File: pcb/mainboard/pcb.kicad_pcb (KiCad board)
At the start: 4 copper layers, 67 x 58 mm, 146 parts, among them J101 Conn_01x04, J400 AudioJack3_SwitchT, J801 USB_B_Mini, U1 AXP209, U201 MIMXRT1176DVMAA, U400 CS43130, U401 ADP150-1.8, U402 ADP150-1.8, U404 MT48H16M32LFB5-6 or IS42VM321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, U700 W25Q128JVP, U800 USBLC6-2P6, Y100 24MHz, Y101 32.768K, Y400 22.5792MHz

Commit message: Mainboard schematics WIP
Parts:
- removed BT1: Conn_01x02, Connector_Molex:Molex_PicoBlade_53261-0271_1x02-1MP_P1.25mm_Horizontal
- removed C1, C10, C11, C12, C14, C15, C17, C18, C2, C214, C23, C3, C400, C423, C837, C9: 10uF, Capacitor_SMD:C_0402_1005Metric
- removed C123, C124, C137, C138, C403, C404: 18pF, Capacitor_SMD:C_0402_1005Metric
- removed C125, C128, C129, C130, C211, C215, C216, C217, C222, C407, C408, C411, C412, C413, C414, C415, C416, C421, C422, C801, C802: 2.2uF, Capacitor_SMD:C_0402_1005Metric
- removed C13, C16: 1nF, Capacitor_SMD:C_0402_1005Metric
- removed C133, C134, C202, C204, C221, C4, C417, C418, C6, C601, C602, C901, C902, C903: 1uF, Capacitor_SMD:C_0402_1005Metric
- removed C135, C206, C5, C703: 470nF, Capacitor_SMD:C_0402_1005Metric
- removed C136, C20, C201, C207, C218, C219, C220, C401, C402, C405, C424, C425, C426, C427, C428, C429, C430, C702, C8: 100nF, Capacitor_SMD:C_0402_1005Metric
- removed C19, C203, C205, C208, C209, C21, C210, C22, C406, C419, C420, C7: 4.7uF, Capacitor_SMD:C_0402_1005Metric
- removed C212: 47uF, Capacitor_SMD:C_0603_1608Metric
- removed C213, C701: 22uF, Capacitor_SMD:C_0603_1608Metric
- removed C409, C410: 15uF, Capacitor_SMD:C_0603_1608Metric
- removed CARD700: MICRO_SD(TFC-WPAPR-08), footprint:TFC-WPAPR-08
- removed D1: LED, Diode_SMD:D_0603_1608Metric
- removed J101: Conn_01x04, Connector_PinHeader_1.27mm:PinHeader_1x04_P1.27mm_Vertical_SMD_Pin1Left
- removed J400: AudioJack3_SwitchT, footprint:PJ-327E
- removed J801: USB_B_Mini, Connector_USB:USB_Mini-B_Wuerth_65100516121_Horizontal
- removed L1, L2, L3: 4.7uH, Inductor_SMD:L_1008_2520Metric
- removed L201: LQH3NPN4R7MGRL, Inductor_SMD:L_Vishay_IHLP-1212
- removed L202, L601, L901, L902: 120R, Inductor_SMD:L_0402_1005Metric
- removed L800: EXC14CE900U, footprint:L_CommonModeChoke_Panasonic_EXC14CE
- removed L802: 300R, Inductor_SMD:L_0603_1608Metric
- removed R1, R3: 1K, Resistor_SMD:R_0402_1005Metric
- removed R102, R103, R104, R105, R202: 4.7K, Resistor_SMD:R_0402_1005Metric
- removed R2: 200K, Resistor_SMD:R_0402_1005Metric
- removed R201: 30K, Resistor_SMD:R_0402_1005Metric
- removed R4: 0.03R, Resistor_SMD:R_0805_2012Metric
- removed R400, R401, R402: 33, Resistor_SMD:R_0402_1005Metric
- removed R403, R700: 0, Resistor_SMD:R_0402_1005Metric
- removed R5: 1R, Resistor_SMD:R_0603_1608Metric
- removed R701: 100K, Capacitor_SMD:C_0402_1005Metric
- removed TH1: 100K, Resistor_SMD:R_0603_1608Metric
- removed TP401, TP402: TestPoint, footprint:TestPoint_Pad_D0.5mm
- removed U1: AXP209, Package_DFN_QFN:QFN-48-1EP_6x6mm_P0.4mm_EP4.2x4.2mm_ThermalVias
- removed U201: MIMXRT1176DVMAA, footprint:BGA-289_17x17_14.0x14.0mm
- removed U400: CS43130, Package_DFN_QFN:QFN-40-1EP_5x5mm_P0.4mm_EP3.6x3.6mm_ThermalVias
- removed U401, U402: ADP150-1.8, footprint:CSP-4_2x2_0.8x0.8mm
- removed U404: MT48H16M32LFB5-6 or IS42VM32160E-6 or W989D2DBJX6, footprint:BGA-90_9x15_8.0x13.0mm
- removed U700: W25Q128JVP, Package_SON:WSON-8-1EP_6x5mm_P1.27mm_EP3.4x4.3mm
- removed U800: USBLC6-2P6, Package_TO_SOT_SMD:SOT-666
- removed Y100: 24MHz, Oscillator:Oscillator_SMD_Abracon_ASE-4Pin_3.2x2.5mm
- removed Y101: 32.768K, Crystal:Crystal_SMD_TXC_9HT11-2Pin_2.0x1.2mm_HandSoldering
- removed Y400: 22.5792MHz, Oscillator:Oscillator_SMD_Abracon_ASE-4Pin_3.2x2.5mm

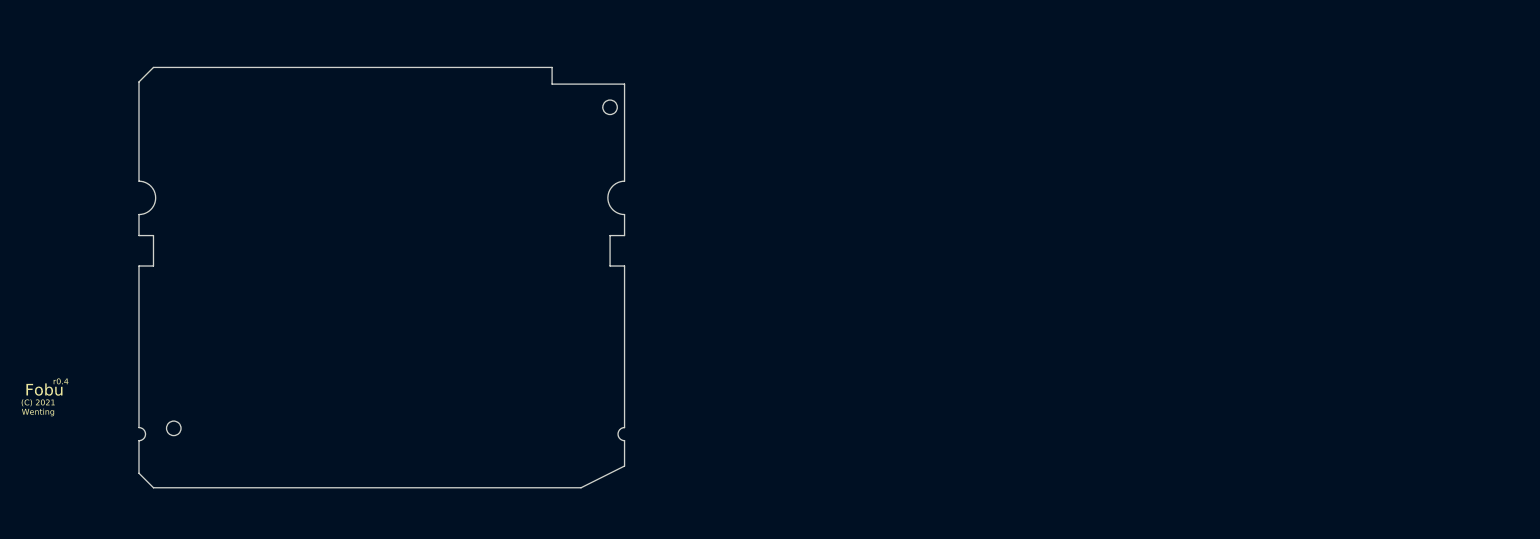
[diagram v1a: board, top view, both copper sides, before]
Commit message: Draft motherboard schematics for r0.0 layout
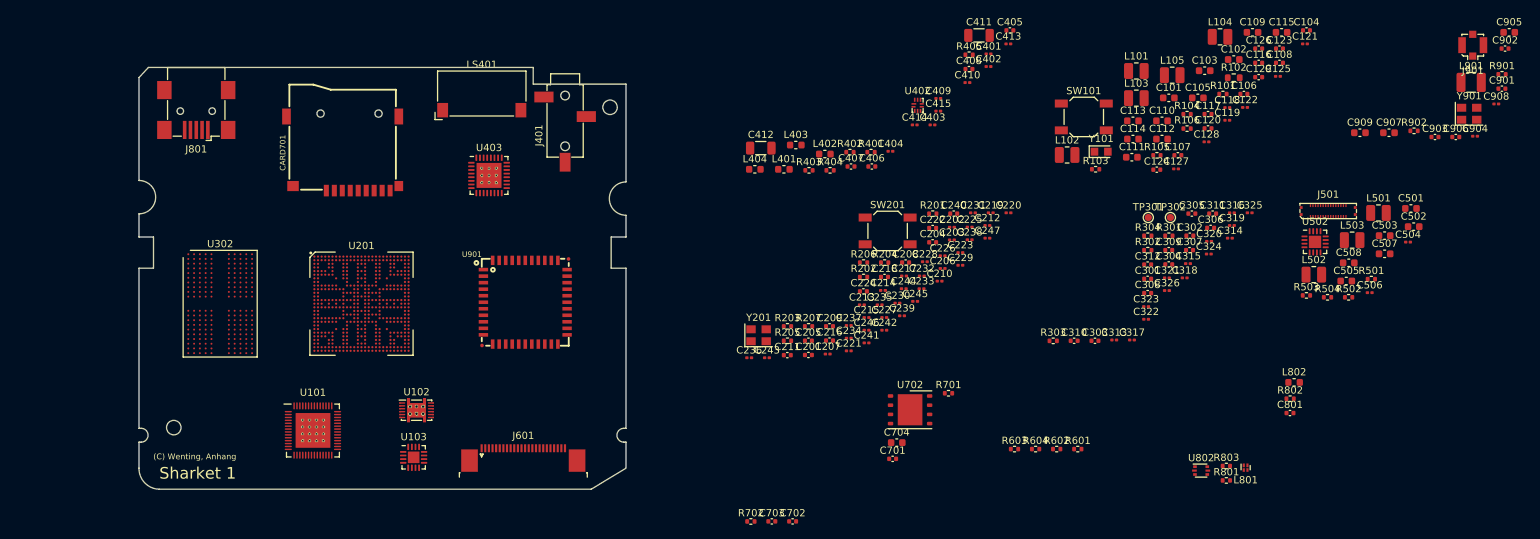
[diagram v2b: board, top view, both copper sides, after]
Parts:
- added C101: 10uF, Capacitor_SMD:C_0603_1608Metric, F.Cu at (260.7, 72.9)
- added C102: 10uF, Capacitor_SMD:C_0603_1608Metric, F.Cu at (269.7, 67.6)
- added C103: 10uF, Capacitor_SMD:C_0603_1608Metric, F.Cu at (265.6, 69.2)
- added C104: 4.7uF, Capacitor_SMD:C_0402_1005Metric, F.Cu at (279.7, 63.6)
- added C105: 10uF, Capacitor_SMD:C_0603_1608Metric, F.Cu at (264.7, 72.9)
- added C106: 4.7uF, Capacitor_SMD:C_0402_1005Metric, F.Cu at (271.1, 72.4)
- added C107: 1uF, Capacitor_SMD:C_0402_1005Metric, F.Cu at (261.9, 80.8)
- added C108: 1uF, Capacitor_SMD:C_0402_1005Metric, F.Cu at (276.0, 68.1)
- added C109: 22uF, Capacitor_SMD:C_0603_1608Metric, F.Cu at (272.2, 63.9)
- added C110: 22uF, Capacitor_SMD:C_0603_1608Metric, F.Cu at (259.8, 76.1)
- added C111: 22uF, Capacitor_SMD:C_0603_1608Metric, F.Cu at (255.6, 81.1)
- added C112: 22uF, Capacitor_SMD:C_0603_1608Metric, F.Cu at (259.8, 78.6)
- added C113: 22uF, Capacitor_SMD:C_0603_1608Metric, F.Cu at (255.8, 76.1)
- added C114: 22uF, Capacitor_SMD:C_0603_1608Metric, F.Cu at (255.8, 78.6)
- added C115: 22uF, Capacitor_SMD:C_0603_1608Metric, F.Cu at (276.3, 63.9)
- added C116: 1uF, Capacitor_SMD:C_0402_1005Metric, F.Cu at (273.1, 68.1)
- added C117: 4.7uF, Capacitor_SMD:C_0402_1005Metric, F.Cu at (266.1, 75.1)
- added C118: 1uF, Capacitor_SMD:C_0201_0603Metric, F.Cu at (268.8, 74.2)
- added C119: 1uF, Capacitor_SMD:C_0201_0603Metric, F.Cu at (268.8, 76.0)
- added C120: 2.2uF, Capacitor_SMD:C_0402_1005Metric, F.Cu at (266.1, 77.1)
- added C121: 1uF, Capacitor_SMD:C_0201_0603Metric, F.Cu at (279.5, 65.5)
- added C122: 1uF, Capacitor_SMD:C_0201_0603Metric, F.Cu at (271.2, 74.2)
- added C123: 1uF, Capacitor_SMD:C_0402_1005Metric, F.Cu at (276.0, 66.1)
- added C124: 18pF, Capacitor_SMD:C_0402_1005Metric, F.Cu at (259.0, 82.8)
- added C125: 1uF, Capacitor_SMD:C_0201_0603Metric, F.Cu at (275.8, 69.9)
- added C126: 18pF, Capacitor_SMD:C_0402_1005Metric, F.Cu at (273.1, 66.1)
- added C127: 1uF, Capacitor_SMD:C_0201_0603Metric, F.Cu at (261.7, 82.7)
- added C128: 1uF, Capacitor_SMD:C_0201_0603Metric, F.Cu at (265.9, 79.0)
- added C129: 4.7uF, Capacitor_SMD:C_0402_1005Metric, F.Cu at (273.1, 70.0)
- added C201: 2.2nF, Capacitor_SMD:C_0402_1005Metric, F.Cu at (211.0, 108.4)
- added C202: 220nF, Capacitor_SMD:C_0201_0603Metric, F.Cu at (230.8, 90.8)
- added C203: 220nF, Capacitor_SMD:C_0201_0603Metric, F.Cu at (230.8, 92.5)
- added C204: 4.7uF, Capacitor_SMD:C_0402_1005Metric, F.Cu at (228.1, 92.8)
- added C205: 10uF, Capacitor_SMD:C_0402_1005Metric, F.Cu at (211.0, 106.4)
- added C206: 220nF, Capacitor_SMD:C_0201_0603Metric, F.Cu at (229.5, 96.4)
- added C207: 220nF, Capacitor_SMD:C_0201_0603Metric, F.Cu at (213.6, 108.2)
- added C208: 10uF, Capacitor_SMD:C_0402_1005Metric, F.Cu at (224.4, 95.6)
- added C209: 1uF, Capacitor_SMD:C_0402_1005Metric, F.Cu at (213.9, 104.4)
- added C210: 1uF, Capacitor_SMD:C_0201_0603Metric, F.Cu at (229.1, 98.2)
- added C211: 1uF, Capacitor_SMD:C_0402_1005Metric, F.Cu at (208.1, 108.4)
- added C212: 220nF, Capacitor_SMD:C_0201_0603Metric, F.Cu at (235.7, 90.5)
- added C213: 220nF, Capacitor_SMD:C_0201_0603Metric, F.Cu at (218.3, 101.5)
- added C214: 1uF, Capacitor_SMD:C_0201_0603Metric, F.Cu at (221.3, 99.5)
- added C215: 1uF, Capacitor_SMD:C_0201_0603Metric, F.Cu at (219.0, 103.2)
- added C216: 1uF, Capacitor_SMD:C_0402_1005Metric, F.Cu at (213.9, 106.4)
- added C217: 220nF, Capacitor_SMD:C_0201_0603Metric, F.Cu at (224.2, 97.5)
- added C218: 18pF, Capacitor_SMD:C_0402_1005Metric, F.Cu at (221.5, 97.6)
- added C219: 220nF, Capacitor_SMD:C_0201_0603Metric, F.Cu at (236.1, 88.8)
- added C220: 1uF, Capacitor_SMD:C_0201_0603Metric, F.Cu at (238.6, 88.8)
- added C221: 1uF, Capacitor_SMD:C_0201_0603Metric, F.Cu at (216.5, 107.8)
- added C222: 1uF, Capacitor_SMD:C_0402_1005Metric, F.Cu at (228.1, 90.9)
- added C223: 220nF, Capacitor_SMD:C_0201_0603Metric, F.Cu at (231.9, 94.2)
- added C224: 18pF, Capacitor_SMD:C_0402_1005Metric, F.Cu at (218.6, 99.6)
- added C225: 220nF, Capacitor_SMD:C_0201_0603Metric, F.Cu at (233.2, 90.7)
- added C226: 1uF, Capacitor_SMD:C_0201_0603Metric, F.Cu at (229.5, 94.7)
- added C227: 1uF, Capacitor_SMD:C_0201_0603Metric, F.Cu at (221.4, 103.2)
- added C228: 220nF, Capacitor_SMD:C_0201_0603Metric, F.Cu at (227.0, 95.5)
- added C229: 1uF, Capacitor_SMD:C_0201_0603Metric, F.Cu at (231.9, 96.0)
- added C230: 1uF, Capacitor_SMD:C_0201_0603Metric, F.Cu at (223.2, 101.2)
- added C231: 220nF, Capacitor_SMD:C_0201_0603Metric, F.Cu at (233.7, 88.8)
- added C232: 1uF, Capacitor_SMD:C_0201_0603Metric, F.Cu at (226.6, 97.5)
- added C233: 1uF, Capacitor_SMD:C_0201_0603Metric, F.Cu at (226.6, 99.2)
- added C234: 220nF, Capacitor_SMD:C_0201_0603Metric, F.Cu at (216.5, 106.1)
- added C235: 220nF, Capacitor_SMD:C_0201_0603Metric, F.Cu at (220.8, 101.5)
- added C236: 1uF, Capacitor_SMD:C_0201_0603Metric, F.Cu at (202.8, 108.8)
- added C237: 220nF, Capacitor_SMD:C_0201_0603Metric, F.Cu at (216.5, 104.3)
- added C238: 220nF, Capacitor_SMD:C_0201_0603Metric, F.Cu at (233.2, 92.5)
- added C239: 1uF, Capacitor_SMD:C_0201_0603Metric, F.Cu at (223.9, 103.0)
- added C240: 10uF, Capacitor_SMD:C_0402_1005Metric, F.Cu at (231.0, 88.9)
- added C241: 220nF, Capacitor_SMD:C_0201_0603Metric, F.Cu at (219.0, 106.7)
- added C242: 1uF, Capacitor_SMD:C_0201_0603Metric, F.Cu at (221.4, 105.0)
- added C243: 220nF, Capacitor_SMD:C_0201_0603Metric, F.Cu at (205.2, 108.8)
- added C244: 220nF, Capacitor_SMD:C_0201_0603Metric, F.Cu at (224.1, 99.2)
- added C245: 1uF, Capacitor_SMD:C_0201_0603Metric, F.Cu at (225.7, 101.0)
- added C246: 220nF, Capacitor_SMD:C_0201_0603Metric, F.Cu at (219.0, 105.0)
- added C247: 1uF, Capacitor_SMD:C_0201_0603Metric, F.Cu at (235.7, 92.3)
- added C301: 10uF, Capacitor_SMD:C_0402_1005Metric, F.Cu at (257.8, 97.9)
- added C302: 10uF, Capacitor_SMD:C_0402_1005Metric, F.Cu at (263.6, 91.9)
- added C303: 10uF, Capacitor_SMD:C_0402_1005Metric, F.Cu at (250.5, 106.4)
- added C304: 10uF, Capacitor_SMD:C_0402_1005Metric, F.Cu at (260.7, 95.9)
- added C305: 10uF, Capacitor_SMD:C_0402_1005Metric, F.Cu at (263.9, 88.9)
- added C306: 10uF, Capacitor_SMD:C_0402_1005Metric, F.Cu at (266.5, 90.8)
- added C307: 10uF, Capacitor_SMD:C_0402_1005Metric, F.Cu at (263.6, 93.9)
- added C308: 10uF, Capacitor_SMD:C_0402_1005Metric, F.Cu at (257.8, 99.8)
- added C309: 10uF, Capacitor_SMD:C_0402_1005Metric, F.Cu at (260.7, 93.9)
- added C310: 10uF, Capacitor_SMD:C_0402_1005Metric, F.Cu at (247.6, 106.4)
- added C311: 10uF, Capacitor_SMD:C_0402_1005Metric, F.Cu at (266.8, 88.9)
- added C312: 10uF, Capacitor_SMD:C_0402_1005Metric, F.Cu at (257.8, 95.9)
- added C313: 220nF, Capacitor_SMD:C_0201_0603Metric, F.Cu at (253.2, 106.3)
- added C314: 220nF, Capacitor_SMD:C_0201_0603Metric, F.Cu at (269.1, 92.3)
- added C315: 220nF, Capacitor_SMD:C_0201_0603Metric, F.Cu at (263.4, 95.8)
- added C316: 220nF, Capacitor_SMD:C_0201_0603Metric, F.Cu at (269.4, 88.8)
- added C317: 220nF, Capacitor_SMD:C_0201_0603Metric, F.Cu at (255.6, 106.3)
- added C318: 220nF, Capacitor_SMD:C_0201_0603Metric, F.Cu at (262.9, 97.7)
- added C319: 220nF, Capacitor_SMD:C_0201_0603Metric, F.Cu at (269.4, 90.5)
- added C320: 220nF, Capacitor_SMD:C_0201_0603Metric, F.Cu at (266.3, 92.7)
- added C321: 220nF, Capacitor_SMD:C_0201_0603Metric, F.Cu at (260.4, 97.7)
- added C322: 220nF, Capacitor_SMD:C_0201_0603Metric, F.Cu at (257.6, 103.5)
- added C323: 220nF, Capacitor_SMD:C_0201_0603Metric, F.Cu at (257.6, 101.7)
- added C324: 220nF, Capacitor_SMD:C_0201_0603Metric, F.Cu at (266.2, 94.5)
- added C325: 220nF, Capacitor_SMD:C_0201_0603Metric, F.Cu at (271.9, 88.8)
- added C326: 220nF, Capacitor_SMD:C_0201_0603Metric, F.Cu at (260.4, 99.5)
- added C401: 220nF, Capacitor_SMD:C_0201_0603Metric, F.Cu at (235.8, 66.8)
- added C402: 220nF, Capacitor_SMD:C_0201_0603Metric, F.Cu at (235.8, 68.6)
- added C403: 220nF, Capacitor_SMD:C_0201_0603Metric, F.Cu at (228.1, 76.6)
- added C404: 220nF, Capacitor_SMD:C_0201_0603Metric, F.Cu at (222.3, 80.3)
- added C405: 10uF, Capacitor_SMD:C_0402_1005Metric, F.Cu at (238.8, 63.6)
- added C406: 10uF, Capacitor_SMD:C_0402_1005Metric, F.Cu at (219.7, 82.4)
- added C407: 1uF, Capacitor_SMD:C_0402_1005Metric, F.Cu at (216.8, 82.4)
- added C408: 1uF, Capacitor_SMD:C_0402_1005Metric, F.Cu at (233.1, 68.9)
- added C409: 220nF, Capacitor_SMD:C_0201_0603Metric, F.Cu at (228.9, 73.0)
- added C410: 100nF, Capacitor_SMD:C_0201_0603Metric, F.Cu at (232.9, 70.8)
- added C411: 100uF, Capacitor_SMD:C_1206_3216Metric, F.Cu at (234.5, 64.3)
- added C412: 100uF, Capacitor_SMD:C_1206_3216Metric, F.Cu at (204.4, 79.8)
- added C413: 100nF, Capacitor_SMD:C_0201_0603Metric, F.Cu at (238.6, 65.5)
- added C414: 100nF, Capacitor_SMD:C_0201_0603Metric, F.Cu at (225.6, 76.6)
- added C415: 220nF, Capacitor_SMD:C_0201_0603Metric, F.Cu at (228.9, 74.7)
- added C501: 10uF, Capacitor_SMD:C_0603_1608Metric, F.Cu at (294.1, 88.2)
- added C502: 10uF, Capacitor_SMD:C_0603_1608Metric, F.Cu at (294.5, 90.7)
- added C503: 10uF, Capacitor_SMD:C_0603_1608Metric, F.Cu at (290.5, 91.9)
- added C504: 100nF, Capacitor_SMD:C_0201_0603Metric, F.Cu at (293.7, 92.8)
- added C505: 10uF, Capacitor_SMD:C_0603_1608Metric, F.Cu at (285.2, 98.2)
- added C506: 100nF, Capacitor_SMD:C_0201_0603Metric, F.Cu at (288.4, 99.8)
- added C507: 10uF, Capacitor_SMD:C_0603_1608Metric, F.Cu at (290.5, 94.4)
- added C508: 10uF, Capacitor_SMD:C_0603_1608Metric, F.Cu at (285.5, 95.7)
- added C701: 18pF, Capacitor_SMD:C_0402_1005Metric, F.Cu at (222.6, 122.7)
- added C702: 470nF, Capacitor_SMD:C_0402_1005Metric, F.Cu at (208.8, 131.3)
- added C703: 1uF, Capacitor_SMD:C_0402_1005Metric, F.Cu at (205.9, 131.3)
- added C704: 22uF, Capacitor_SMD:C_0603_1608Metric, F.Cu at (223.2, 120.5)
- added C801: 10uF, Capacitor_SMD:C_0402_1005Metric, F.Cu at (277.4, 116.4)
- added C901: 18pF, Capacitor_SMD:C_0402_1005Metric, F.Cu at (306.7, 71.6)
- added C902: 18pF, Capacitor_SMD:C_0402_1005Metric, F.Cu at (307.1, 66.1)
- added C903: DNP, Capacitor_SMD:C_0402_1005Metric, F.Cu at (297.4, 78.3)
- added C904: 100nF, Capacitor_SMD:C_0201_0603Metric, F.Cu at (303.0, 78.2)
- added C905: 10uF, Capacitor_SMD:C_0603_1608Metric, F.Cu at (307.7, 63.9)
- added C906: DNP, Capacitor_SMD:C_0402_1005Metric, F.Cu at (300.3, 78.3)
- added C907: 10uF, Capacitor_SMD:C_0603_1608Metric, F.Cu at (291.1, 77.7)
- added C908: 100nF, Capacitor_SMD:C_0201_0603Metric, F.Cu at (305.9, 73.7)
- added C909: 10uF, Capacitor_SMD:C_0603_1608Metric, F.Cu at (287.1, 77.7)
- added CARD701: MICRO_SD(TFC-WPAPR-08), footprint:TFC-WPAPR-08, F.Cu at (146.7, 78.3)
- added J401: AudioJack3, footprint:PJ-208, F.Cu at (177.4, 76.1)
- added J501: Conn_02x15_Odd_Even_MountingPin, footprint:505270-3012, F.Cu at (282.7, 88.5)
- added J601: Conn_01x24_MountingPin, Connector_FFC-FPC:TE_2-1734839-4_1x24-1MP_P0.5mm_Horizontal, F.Cu at (171.6, 122.6)
- added J801: USB_B_Mini, Connector_USB:USB_Mini-B_Wuerth_65100516121_Horizontal, F.Cu at (126.5, 74.7)
- added J901: U.FL Connector, Connector_Coaxial:U.FL_Molex_MCRF_73412-0110_Vertical, F.Cu at (302.6, 65.6)
- added L101: 470nH, Inductor_SMD:L_1008_2520Metric, F.Cu at (256.2, 69.2)
- added L102: 470nH, Inductor_SMD:L_1008_2520Metric, F.Cu at (246.7, 80.8)
- added L103: 470nH, Inductor_SMD:L_1008_2520Metric, F.Cu at (256.2, 72.9)
- added L104: 470nH, Inductor_SMD:L_1008_2520Metric, F.Cu at (267.8, 64.5)
- added L105: 470nH, Inductor_SMD:L_1008_2520Metric, F.Cu at (261.2, 69.8)
- added L401: 120R, Inductor_SMD:L_0603_1608Metric, F.Cu at (207.6, 82.8)
- added L402: 120R, Inductor_SMD:L_0603_1608Metric, F.Cu at (213.2, 80.7)
- added L403: 15uH, Inductor_SMD:L_0603_1608Metric, F.Cu at (209.2, 79.4)
- added L404: 15uH, Inductor_SMD:L_0603_1608Metric, F.Cu at (203.6, 82.8)
- added L501: 10uH, Inductor_SMD:L_1008_2520Metric, F.Cu at (289.6, 88.8)
- added L502: 4.7uH, Inductor_SMD:L_1008_2520Metric, F.Cu at (280.7, 97.3)
- added L503: 4.7uH, Inductor_SMD:L_1008_2520Metric, F.Cu at (286.0, 92.5)
- added L801: EXC14CE900U, footprint:L_CommonModeChoke_Panasonic_EXC14CE, F.Cu at (271.3, 123.9)
- added L802: 120R, Inductor_SMD:L_0603_1608Metric, F.Cu at (278.0, 112.2)
- added L901: 4.7uH, Inductor_SMD:L_1210_3225Metric, F.Cu at (302.4, 70.8)
- added LS401: Speaker, Buzzer_Beeper:Speaker_CUI_CMR-1206S-67, F.Cu at (165.9, 72.3)
- added R101: 0, Resistor_SMD:R_0402_1005Metric, F.Cu at (268.2, 72.4)
- added R102: 0.01/1%, Resistor_SMD:R_0603_1608Metric, F.Cu at (269.7, 70.1)
- added R103: 10K, Resistor_SMD:R_0402_1005Metric, F.Cu at (250.6, 82.8)
- added R104: 10K, Resistor_SMD:R_0402_1005Metric, F.Cu at (263.2, 75.2)
- added R105: 2K, Resistor_SMD:R_0402_1005Metric, F.Cu at (259.1, 80.8)
- added R106: 1K, Resistor_SMD:R_0402_1005Metric, F.Cu at (263.2, 77.1)
- added R201: 10K, Resistor_SMD:R_0402_1005Metric, F.Cu at (228.1, 88.9)
- added R202: 100K/1%, Resistor_SMD:R_0402_1005Metric, F.Cu at (218.6, 97.6)
- added R203: 100K, Resistor_SMD:R_0402_1005Metric, F.Cu at (208.1, 104.4)
- added R204: 10K, Resistor_SMD:R_0402_1005Metric, F.Cu at (221.5, 95.6)
- added R205: 10K, Resistor_SMD:R_0402_1005Metric, F.Cu at (208.1, 106.4)
- added R206: 10K, Resistor_SMD:R_0402_1005Metric, F.Cu at (218.6, 95.6)
- added R207: 10K, Resistor_SMD:R_0402_1005Metric, F.Cu at (211.0, 104.4)
- added R301: 10K, Resistor_SMD:R_0402_1005Metric, F.Cu at (260.7, 91.9)
- added R302: 240/1%, Resistor_SMD:R_0402_1005Metric, F.Cu at (257.8, 93.9)
- added R303: 150/1%, Resistor_SMD:R_0402_1005Metric, F.Cu at (244.8, 106.4)
- added R304: 240/1%, Resistor_SMD:R_0402_1005Metric, F.Cu at (257.8, 91.9)
- added R401: 22R, Resistor_SMD:R_0402_1005Metric, F.Cu at (219.6, 80.4)
- added R402: 22R, Resistor_SMD:R_0402_1005Metric, F.Cu at (216.7, 80.4)
- added R403: 22R, Resistor_SMD:R_0402_1005Metric, F.Cu at (211.1, 82.9)
- added R404: 22R, Resistor_SMD:R_0402_1005Metric, F.Cu at (214.0, 82.9)
- added R405: 22R, Resistor_SMD:R_0402_1005Metric, F.Cu at (233.1, 67.0)
- added R501: 0, Resistor_SMD:R_0402_1005Metric, F.Cu at (288.6, 97.9)
- added R502: DNP, Resistor_SMD:R_0402_1005Metric, F.Cu at (285.5, 100.4)
- added R503: 0, Resistor_SMD:R_0402_1005Metric, F.Cu at (279.7, 100.2)
- added R504: DNP, Resistor_SMD:R_0402_1005Metric, F.Cu at (282.6, 100.4)
- added R601: 4.7K, Resistor_SMD:R_0402_1005Metric, F.Cu at (248.1, 121.4)
- added R602: 4.7K, Resistor_SMD:R_0402_1005Metric, F.Cu at (245.2, 121.4)
- added R603: 4.7K, Resistor_SMD:R_0402_1005Metric, F.Cu at (239.4, 121.4)
- added R604: 4.7K, Resistor_SMD:R_0402_1005Metric, F.Cu at (242.3, 121.4)
- added R701: 100K, Resistor_SMD:R_0402_1005Metric, F.Cu at (230.3, 113.7)
- added R702: 0, Resistor_SMD:R_0402_1005Metric, F.Cu at (203.0, 131.3)
- added R801: 200/1%, Resistor_SMD:R_0402_1005Metric, F.Cu at (268.6, 125.7)
- added R802: 100K, Resistor_SMD:R_0402_1005Metric, F.Cu at (277.4, 114.4)
- added R803: 100K, Resistor_SMD:R_0402_1005Metric, F.Cu at (268.6, 123.7)
- added R901: 22, Resistor_SMD:R_0402_1005Metric, F.Cu at (306.7, 69.7)
- added R902: 0, Resistor_SMD:R_0402_1005Metric, F.Cu at (294.5, 77.5)
- added SW101: SW_Push, Button_Switch_SMD:SW_SPST_SKQG_WithStem, F.Cu at (249.0, 75.5)
- added SW201: SW_Push, Button_Switch_SMD:SW_SPST_SKQG_WithStem, F.Cu at (221.9, 91.3)
- added TP301: TestPoint, TestPoint:TestPoint_Pad_D1.0mm, F.Cu at (257.9, 89.4)
- added TP302: TestPoint, TestPoint:TestPoint_Pad_D1.0mm, F.Cu at (260.9, 89.4)
- added U101: PCA9450BHN, footprint:QFN-56_EP_7x7_Pitch0.4mm, F.Cu at (142.6, 118.8)
- added U102: BQ27441-G1, Package_SON:Texas_S-PDSO-N12, F.Cu at (156.9, 116.0)
- added U103: BQ24072RGT, Package_DFN_QFN:VQFN-16-1EP_3x3mm_P0.5mm_EP1.6x1.6mm, F.Cu at (156.5, 122.5)
- added U201: MIMX8MN6DVTJZAA, footprint:BGA-486_27x27_14.0x14.0mm, F.Cu at (149.3, 101.3)
- added U302: MT53D512M16D1DS-046, Package_BGA:BGA-200_10.0x14.5mm_Layout12x22_P0.80x0.65mm, F.Cu at (129.8, 101.3)
- added U402: FSA2269UMX, Package_DFN_QFN:UQFN-10_1.4x1.8mm_P0.4mm, F.Cu at (226.0, 73.9)
- added U403: WM8978, Package_DFN_QFN:QFN-32-1EP_5x5mm_P0.5mm_EP3.45x3.45mm_ThermalVias, F.Cu at (166.9, 83.6)
- added U502: TPS65632, Package_DFN_QFN:QFN-16-1EP_3x3mm_P0.5mm_EP1.7x1.7mm, F.Cu at (280.9, 92.8)
- added U702: W25Q128JVP, Package_SON:WSON-8-1EP_6x5mm_P1.27mm_EP3.4x4.3mm, F.Cu at (225.0, 115.9)
- added U802: USBLC6-2P6, Package_TO_SOT_SMD:SOT-666, F.Cu at (265.2, 124.3)
- added U901: AP6330(BCM4330), footprint:RL-SM02BD(RTL8723BS), F.Cu at (171.9, 101.1)
- added Y101: 32.768K, Crystal:Crystal_SMD_TXC_9HT11-2Pin_2.0x1.2mm_HandSoldering, F.Cu at (251.4, 80.3)
- added Y201: 24MHz, Oscillator:Oscillator_SMD_Abracon_ASE-4Pin_3.2x2.5mm, F.Cu at (204.1, 105.7)
- added Y901: 26MHz, Oscillator:Oscillator_SMD_Abracon_ASE-4Pin_3.2x2.5mm, F.Cu at (302.1, 75.1)
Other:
- board size 67 x 58 mm -> 67.2 x 58.2 mm
- board text added: "(C) Wenting, Anhang"
- board text added: "Sharket 1"
- board text removed: "(C) 2021 Wenting"
- board text removed: "Fobu"
- board text removed: "r0.4"

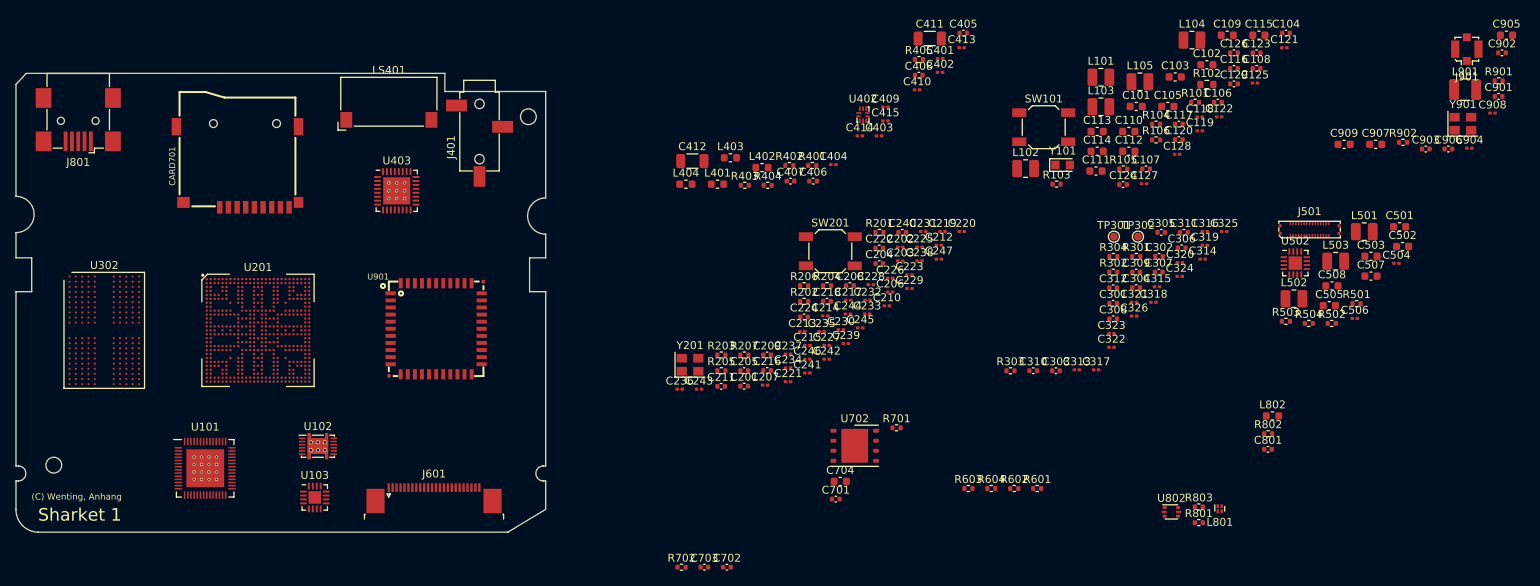
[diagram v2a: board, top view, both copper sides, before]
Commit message: Motherboard PCB component initial placement, schematics fixes
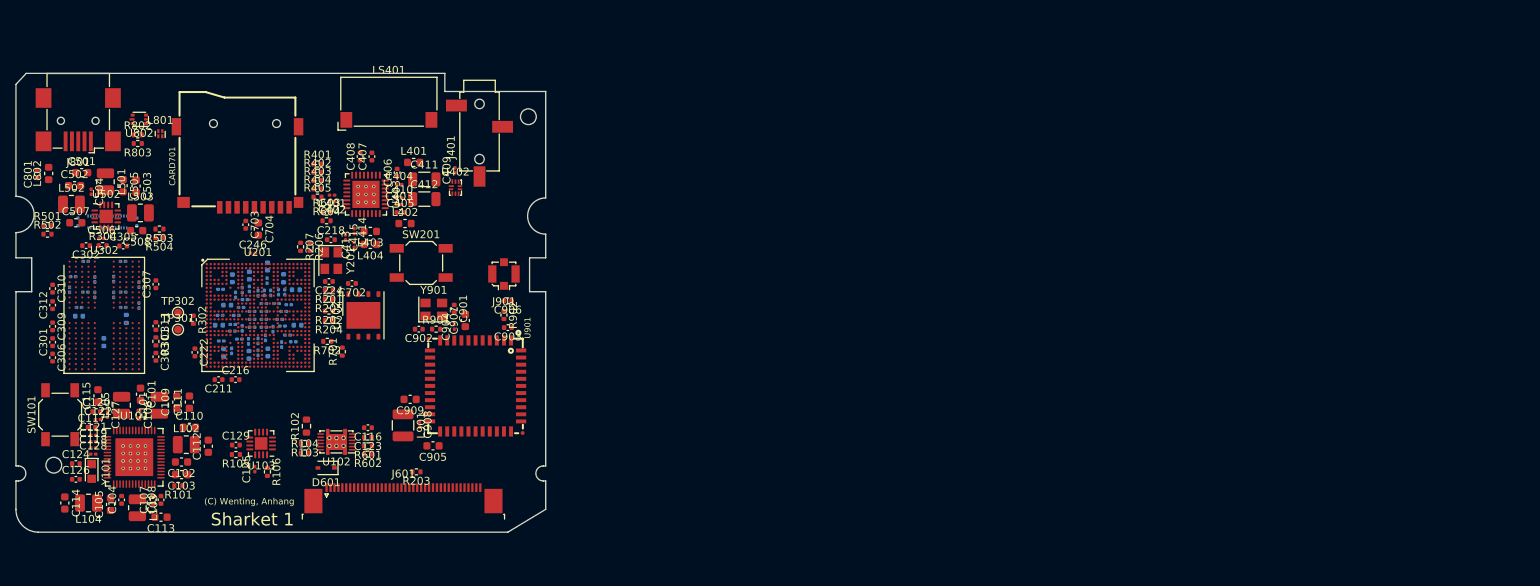
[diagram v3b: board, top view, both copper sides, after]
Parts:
- added C248: 10uF, Capacitor_SMD:C_0402_1005Metric, B.Cu at (144.3, 100.7)
- added C249: 10uF, Capacitor_SMD:C_0402_1005Metric, B.Cu at (145.4, 98.1)
- added C250: 10uF, Capacitor_SMD:C_0402_1005Metric, B.Cu at (146.1, 94.7)
- added C251: 1uF, Capacitor_SMD:C_0201_0603Metric, B.Cu at (146.4, 96.8)
- added C252: 1uF, Capacitor_SMD:C_0201_0603Metric, B.Cu at (144.6, 96.1)
- added C253: 1uF, Capacitor_SMD:C_0201_0603Metric, B.Cu at (146.1, 100.5)
- added C254: 1uF, Capacitor_SMD:C_0201_0603Metric, B.Cu at (147.2, 98.4)
- added C255: 1uF, Capacitor_SMD:C_0201_0603Metric, B.Cu at (146.1, 101.4)
- added D601: TBD, Diode_SMD:D_SOD-323, F.Cu at (157.9, 118.8)
- C201, C202, C203, C204, C205, C206, C207, C208, C210, C212, C213, C214, C215, C217, C219, C220, C221, C223, C225, C226, C227, C228, C229, C230, C231, C232, C233, C234, C235, C236, C237, C238, C239, C240, C241, C242, C243, C244, C245, C247, C304, C308, C313, C314, C315, C316, C317, C318, C319, C320, C321, C322, C323, C324, C325, C326, C701, J501, R303, R801: moved to B.Cu
- C209: value 1uF -> 10uF; moved to B.Cu
- C211, C216, C222: value 1uF -> 10uF
- J601: value Conn_01x24_MountingPin -> Conn_01x40_MountingPin; footprint Connector_FFC-FPC:TE_2-1734839-4_1x24-1MP_P0.5mm_Horizontal -> Connector_FFC-FPC:TE_4-1734839-0_1x40-1MP_P0.5mm_Horizontal
- moved C502 168.6 mm to (126.0, 83.0)
- moved C501 167.3 mm to (126.9, 81.3)
- moved R501 166.4 mm to (122.6, 88.0)
- moved C504 165.8 mm to (128.1, 83.7), turned to -90 degrees
- moved C507 164.4 mm to (126.2, 87.7)
- moved R502 163.3 mm to (122.6, 89.1)
- moved C801 160.0 mm to (121.3, 81.5), turned to 90 degrees
- moved L501 159.8 mm to (129.9, 82.5), turned to -90 degrees
- moved C506 159.3 mm to (129.4, 89.7)
- moved C104 159.1 mm to (132.0, 122.8), turned to 90 degrees
- moved C121 158.9 mm to (128.4, 114.6)
- moved L802 158.3 mm to (122.8, 81.4), turned to 90 degrees
- moved C503 156.9 mm to (133.8, 83.0), turned to -90 degrees
- moved C126 156.5 mm to (126.2, 120.2)
- moved L502 155.5 mm to (125.6, 85.3)
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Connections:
- net /usb/TYPEC_DN renamed /usb/USB_PORT_DN
- net /usb/TYPEC_DP renamed /usb/USB_PORT_DP
- C246 pad 1: +3V3 -> +1V8
- C404 pad 1: Net-(C403-Pad1) -> Net-(C404-Pad1)
- C405 pad 1: Net-(C405-Pad1) -> Net-(C403-Pad1)
- C406 pad 1: Net-(C403-Pad1) -> Net-(C404-Pad1)
- C411 pad 2: unconnected-(C411-Pad2) -> /audio/HP_L
- C412 pad 2: unconnected-(C412-Pad2) -> /audio/HP_R
- C904 pad 1: +3V3 -> +BATT
- C907 pad 1: +3V3 -> +BATT
- C908 pad 1: +3V3 -> +1V8
- C909 pad 1: +3V3 -> +1V8
- CARD701 pad 4: GND -> +SD
- J601 pad 1: unconnected-(J601-Pad1) -> GND
- J601 pad 10: KC6 -> UART4_RXD
- J601 pad 11: KC5 -> UART2_TXD
- J601 pad 12: KC4 -> UART4_TXD
- J601 pad 13: KC3 -> +3V3
- J601 pad 14: KC2 -> GND
- J601 pad 15: KC1 -> +1V8
- J601 pad 16: KC0 -> GND
- J601 pad 17: KR6 -> BATP
- J601 pad 18: KR5 -> BATP
- J601 pad 19: KR4 -> BATP
- J601 pad 2: BATP -> GND
- J601 pad 20: KR3 -> BATP
- J601 pad 21: KR2 -> BATP
- J601 pad 22: KR1 -> GND
- J601 pad 23: KR0 -> GND
- J601 pad 3: BATP -> Net-(D601-Pad1)
- J601 pad 4: BATP -> JTAG_TDI
- J601 pad 5: BATP -> JTAG_TDO
- J601 pad 6: GND -> JTAG_TCK
- J601 pad 7: GND -> JTAG_TMS
- J601 pad 9: ONOFF -> UART2_RXD
- L401 pad 1: Net-(C403-Pad1) -> Net-(C404-Pad1)
- L402 pad 1: Net-(C405-Pad1) -> Net-(C403-Pad1)
- R205 pad 1: RTC_1P8 -> Net-(R205-Pad1)
- R206 pad 1: RTC_1P8 -> Net-(R205-Pad1)
- U101 pad 18: unconnected-(U101-Pad18) -> +BATT
- U101 pad 35: unconnected-(U101-Pad35) -> +BATT
- U201 pad A22: USB_DM -> USB_DN
- U201 pad E26: unconnected-(U201-PadE26) -> JTAG_TDO
- U201 pad E27: unconnected-(U201-PadE27) -> JTAG_TDI
- U201 pad F26: unconnected-(U201-PadF26) -> JTAG_TCK
- U201 pad F27: unconnected-(U201-PadF27) -> JTAG_TMS
- U201 pad J12: +3V3 -> +1V8
- U302 pad A10: Net-(U302-PadA10) -> GND
- U302 pad A3: Net-(U302-PadA10) -> GND
- U302 pad C1: Net-(U302-PadA10) -> GND
- U302 pad C12: Net-(U302-PadA10) -> GND
- U302 pad C5: Net-(U302-PadA10) -> GND
- U302 pad C8: Net-(U302-PadA10) -> GND
- U302 pad D11: Net-(U302-PadA10) -> GND
- U302 pad D2: Net-(U302-PadA10) -> GND
- U302 pad D4: Net-(U302-PadA10) -> GND
- U302 pad D9: Net-(U302-PadA10) -> GND
- U302 pad E1: Net-(U302-PadA10) -> GND
- U302 pad E12: Net-(U302-PadA10) -> GND
- U302 pad E5: Net-(U302-PadA10) -> GND
- U302 pad E8: Net-(U302-PadA10) -> GND
- U302 pad G1: Net-(U302-PadA10) -> GND
- U302 pad G10: Net-(U302-PadA10) -> GND
- U302 pad G12: Net-(U302-PadA10) -> GND
- U302 pad G3: Net-(U302-PadA10) -> GND
- U302 pad G5: Net-(U302-PadA10) -> GND
- U302 pad G8: Net-(U302-PadA10) -> GND
- U302 pad J1: Net-(U302-PadA10) -> GND
- U302 pad J10: Net-(U302-PadA10) -> GND
- U302 pad J12: Net-(U302-PadA10) -> GND
- U302 pad J3: Net-(U302-PadA10) -> GND
- U302 pad K11: Net-(U302-PadA10) -> GND
- U302 pad K2: Net-(U302-PadA10) -> GND
- U302 pad K4: Net-(U302-PadA10) -> GND
- U302 pad K9: Net-(U302-PadA10) -> GND
- U403 pad 31: Net-(C403-Pad1) -> Net-(C404-Pad1)
- U901 pad 22: +3V3 -> +1V8
- U901 pad 9: +3V3 -> +BATT
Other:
- outline, holes or cut-outs redrawn
